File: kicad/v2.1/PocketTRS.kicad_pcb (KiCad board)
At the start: 2 copper layers, 87.6 x 73.9 mm, 40 parts, among them J1 TRS-80, J2 AudioJack3, J3 Mini-DIN-6, J4 DB15_Female_HighDensity, J5 Programmer, J6 USB_B_Micro, J7 PTRS_RESET, J8 ESP_RESET, Q1 BSS138, Q2 MMBT3904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

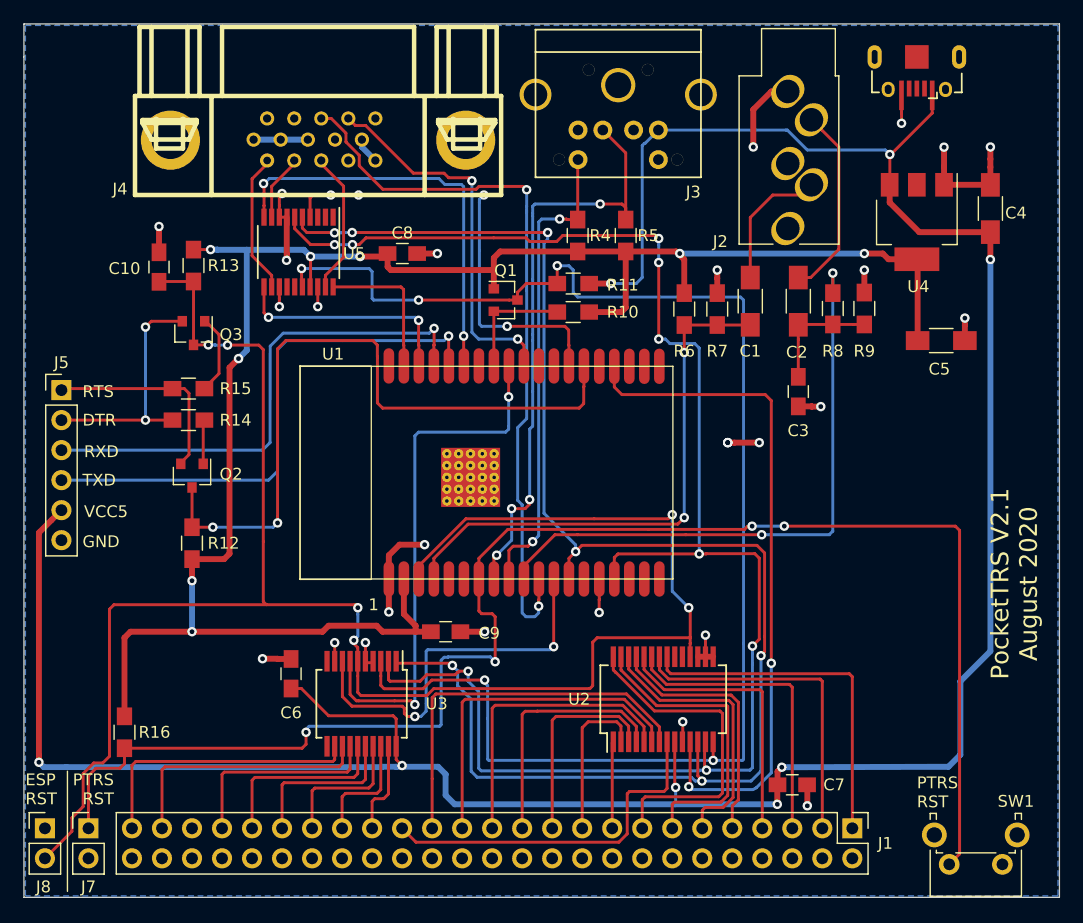
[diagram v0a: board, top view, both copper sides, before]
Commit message: Updated Silk Screen
1. Added labels to indicate pin 1 for U1, U2, U3 and U5.
2. Added + to indicate orientation for C1, C2, C3 and C5
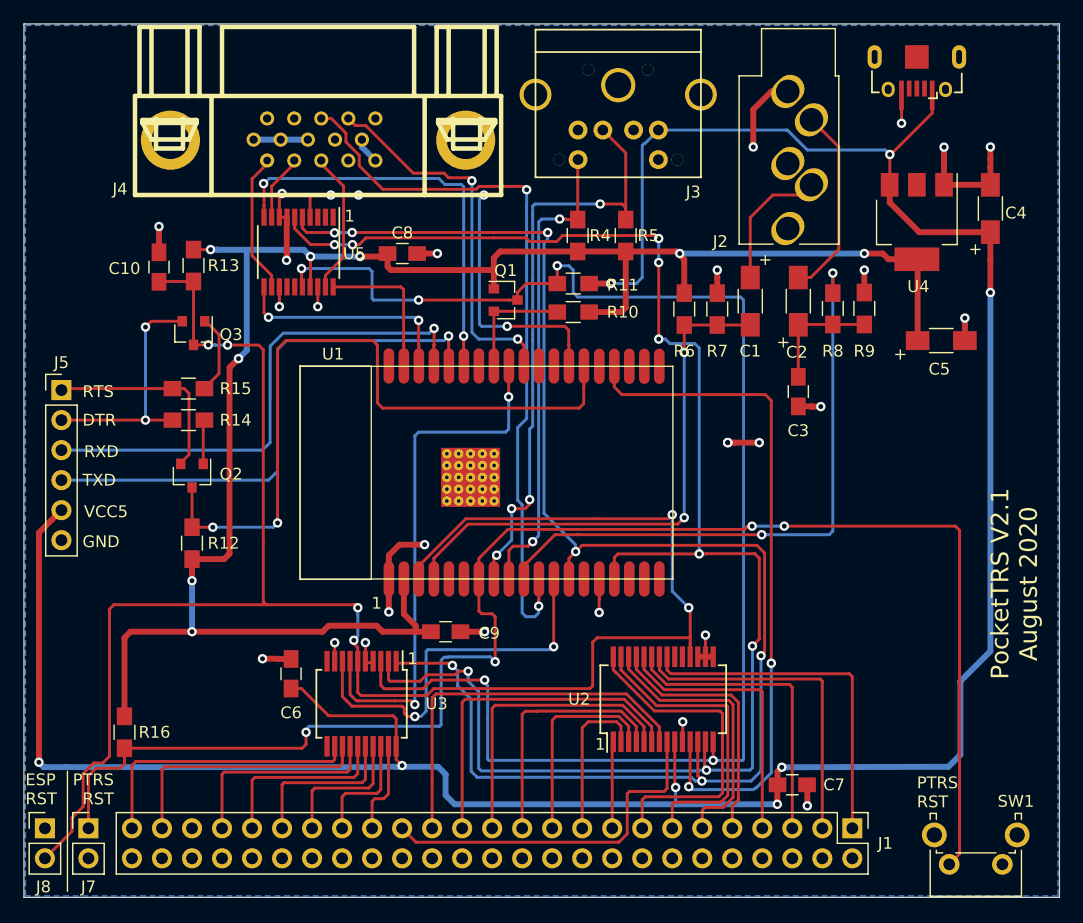
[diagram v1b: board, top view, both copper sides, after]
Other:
- board text added: "+"
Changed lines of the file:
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@@
   (general
     (thickness 1.6)
-    (drawings 18)
-    (tracks 925)
+    (drawings 25)
+    (tracks 926)
     (zones 0)
     (modules 40)
@@
     )
   )
-  (gr_text 1 (at 194.691 111.125) (layer F.SilkS)
+  (gr_text + (at 229.362 88.9) (layer F.SilkS)
+    (effects (font (size 1 1) (thickness 0.15)))
+  )
+  (gr_text + (at 227.838 81.915) (layer F.SilkS)
+    (effects (font (size 1 1) (thickness 0.15)))
+  )
+  (gr_text + (at 239.268 89.916) (layer F.SilkS)
+    (effects (font (size 1 1) (thickness 0.15)))
+  )
+  (gr_text + (at 245.618 81.026) (layer F.SilkS)
+    (effects (font (size 1 1) (thickness 0.15)))
+  )
+  (gr_text 1 (at 192.659 78.232) (layer F.SilkS)
+    (effects (font (size 1 1) (thickness 0.15)))
+  )
+  (gr_text 1 (at 197.993 115.697) (layer F.SilkS)
+    (effects (font (size 1 1) (thickness 0.15)))
+  )
+  (gr_text 1 (at 213.868 122.936) (layer F.SilkS)
+    (effects (font (size 1 1) (thickness 0.15)))
+  )
+  (gr_text 1 (at 194.945 110.998) (layer F.SilkS)
     (effects (font (size 1 1) (thickness 0.15)))
   )
@@
   (segment (start 228.874 126.365) (end 228.874 125.24) (width 0.5) (layer F.Cu) (net 6) (status 10))
   (via (at 229.235 124.879) (size 0.8) (drill 0.4) (layers F.Cu B.Cu) (net 6))
-  (via (at 246.888 81.915) (size 0.8) (drill 0.4) (layers F.Cu B.Cu) (net 6))
   (segment (start 246.888 81.915) (end 246.888 79.597) (width 0.5) (layer F.Cu) (net 6) (status 20))
   (segment (start 168.682 124.867) (end 166.777 124.867) (width 0.5) (layer B.Cu) (net 6))
@@
   (segment (start 244.348 117.602) (end 244.348 123.825) (width 0.5) (layer B.Cu) (net 6))
   (segment (start 246.888 115.062) (end 244.348 117.602) (width 0.5) (layer B.Cu) (net 6))
-  (segment (start 246.888 81.915) (end 246.888 115.062) (width 0.5) (layer B.Cu) (net 6))
   (segment (start 196.596 124.841) (end 195.401 124.841) (width 0.5) (layer B.Cu) (net 6))
   (segment (start 188.581 118.217) (end 190.887 120.523) (width 0.25) (layer F.Cu) (net 6))
@@
   (segment (start 196.6 123.107) (end 196.6 124.232) (width 0.25) (layer F.Cu) (net 6))
   (via (at 197.104 124.736) (size 0.8) (drill 0.4) (layers F.Cu B.Cu) (net 6))
+  (segment (start 246.888 81.915) (end 246.888 84.709) (width 0.5) (layer F.Cu) (net 6))
+  (via (at 246.888 84.709) (size 0.8) (drill 0.4) (layers F.Cu B.Cu) (net 6))
+  (segment (start 246.888 84.709) (end 246.888 115.062) (width 0.5) (layer B.Cu) (net 6))
   (segment (start 211.963 81.233) (end 216.027 81.233) (width 0.5) (layer F.Cu) (net 7) (status 30))
   (segment (start 240.729 81.954) (end 240.665 81.89) (width 0.5) (layer F.Cu) (net 7) (status 30))
